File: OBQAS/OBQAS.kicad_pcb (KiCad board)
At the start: 2 copper layers, 151 x 100 mm, 146 parts, among them J1 24V IN, J2 USB_C_Receptacle_USB2.0, J3 K type, J5 TF_PUSH, J6 CH1, J7 CH2, K1 G5NB-1A-E_DC5, K2 G5NB-1A-E_DC5, K3 G5NB-1A-E_DC5, K4 G5NB-1A-E_DC5, Q1 IRLML2803TRPBF, Q2 IRLML2803TRPBF, Q3 IRLML2803TRPBF, Q4 IRLML2803TRPBF, Q5 BC846, Q6 BC846, Q7 IRLZ44N, Q8 IRLZ44N, Q9 IRFP064, SW1 SW_SPST, SW2 Enc, U1 LM7805_TO220, U2 AMS1117-3.3, U3 ESP32-WROOM-32, U4 CH340C, U5 TPS55288QWRPMRQ1, U6 LM358, U7 LM358, U8 MCP4921, U9 ADS1115IDGS

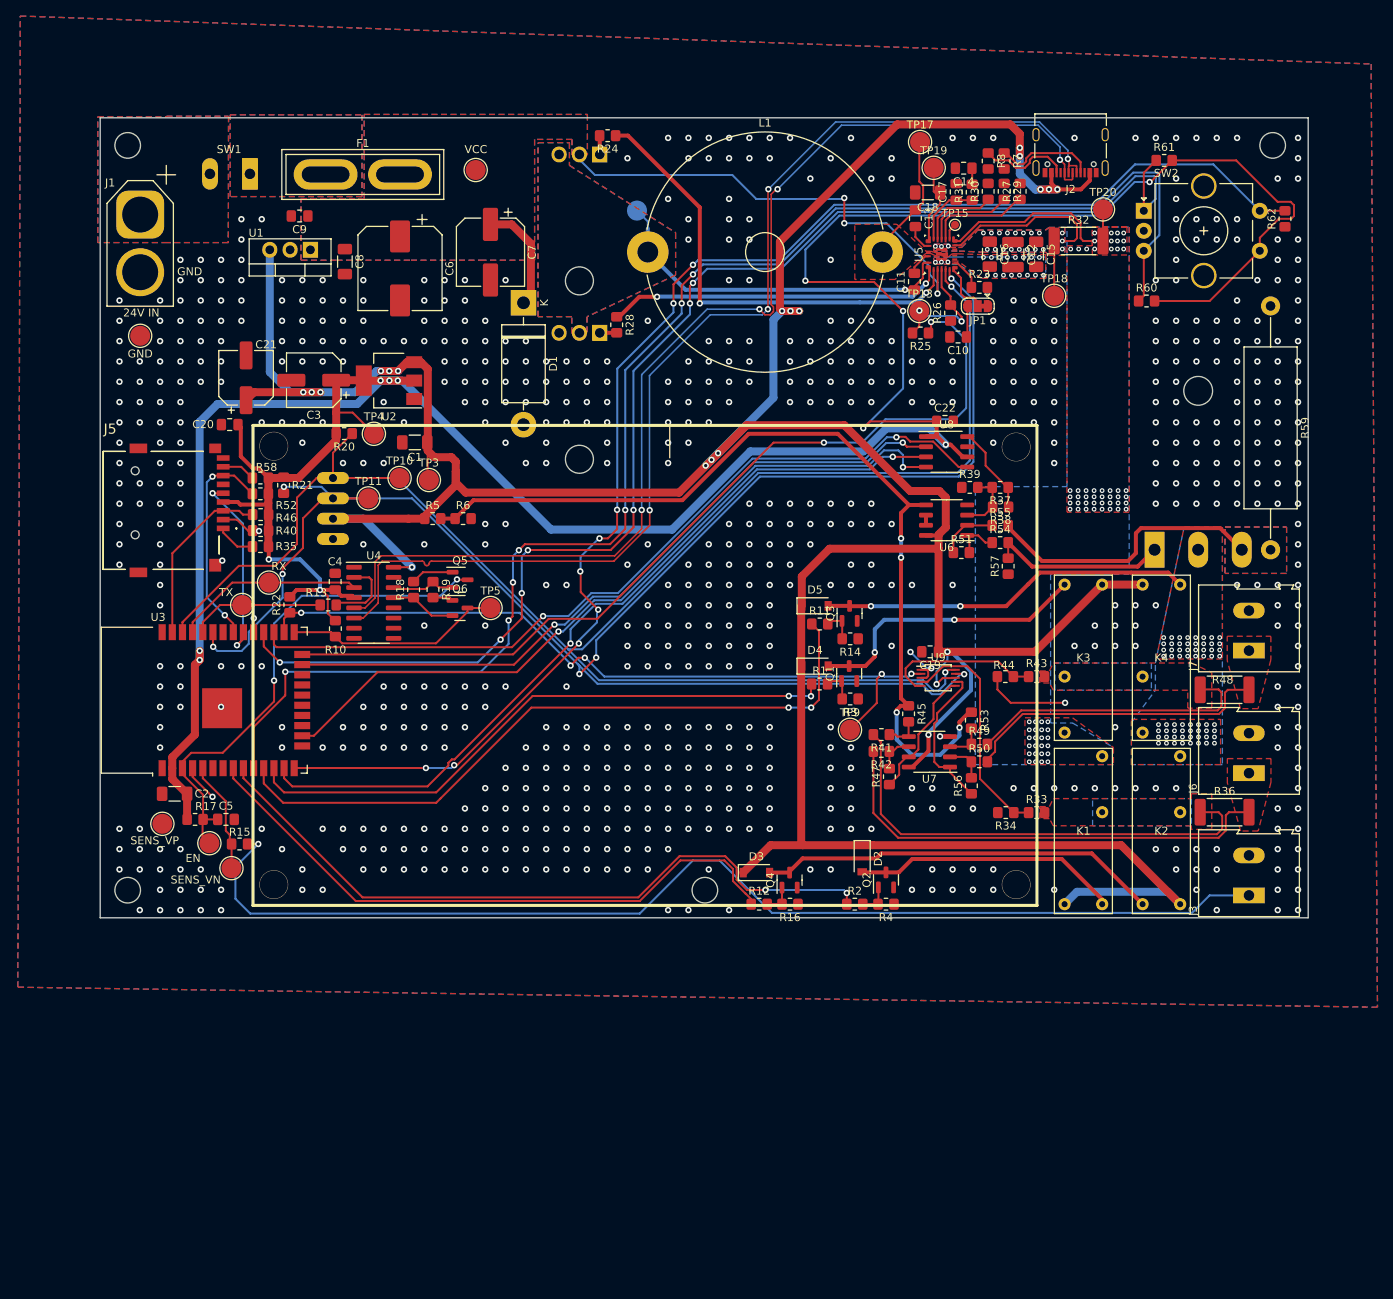
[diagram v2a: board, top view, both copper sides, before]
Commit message: updated schematic with balancing circuit
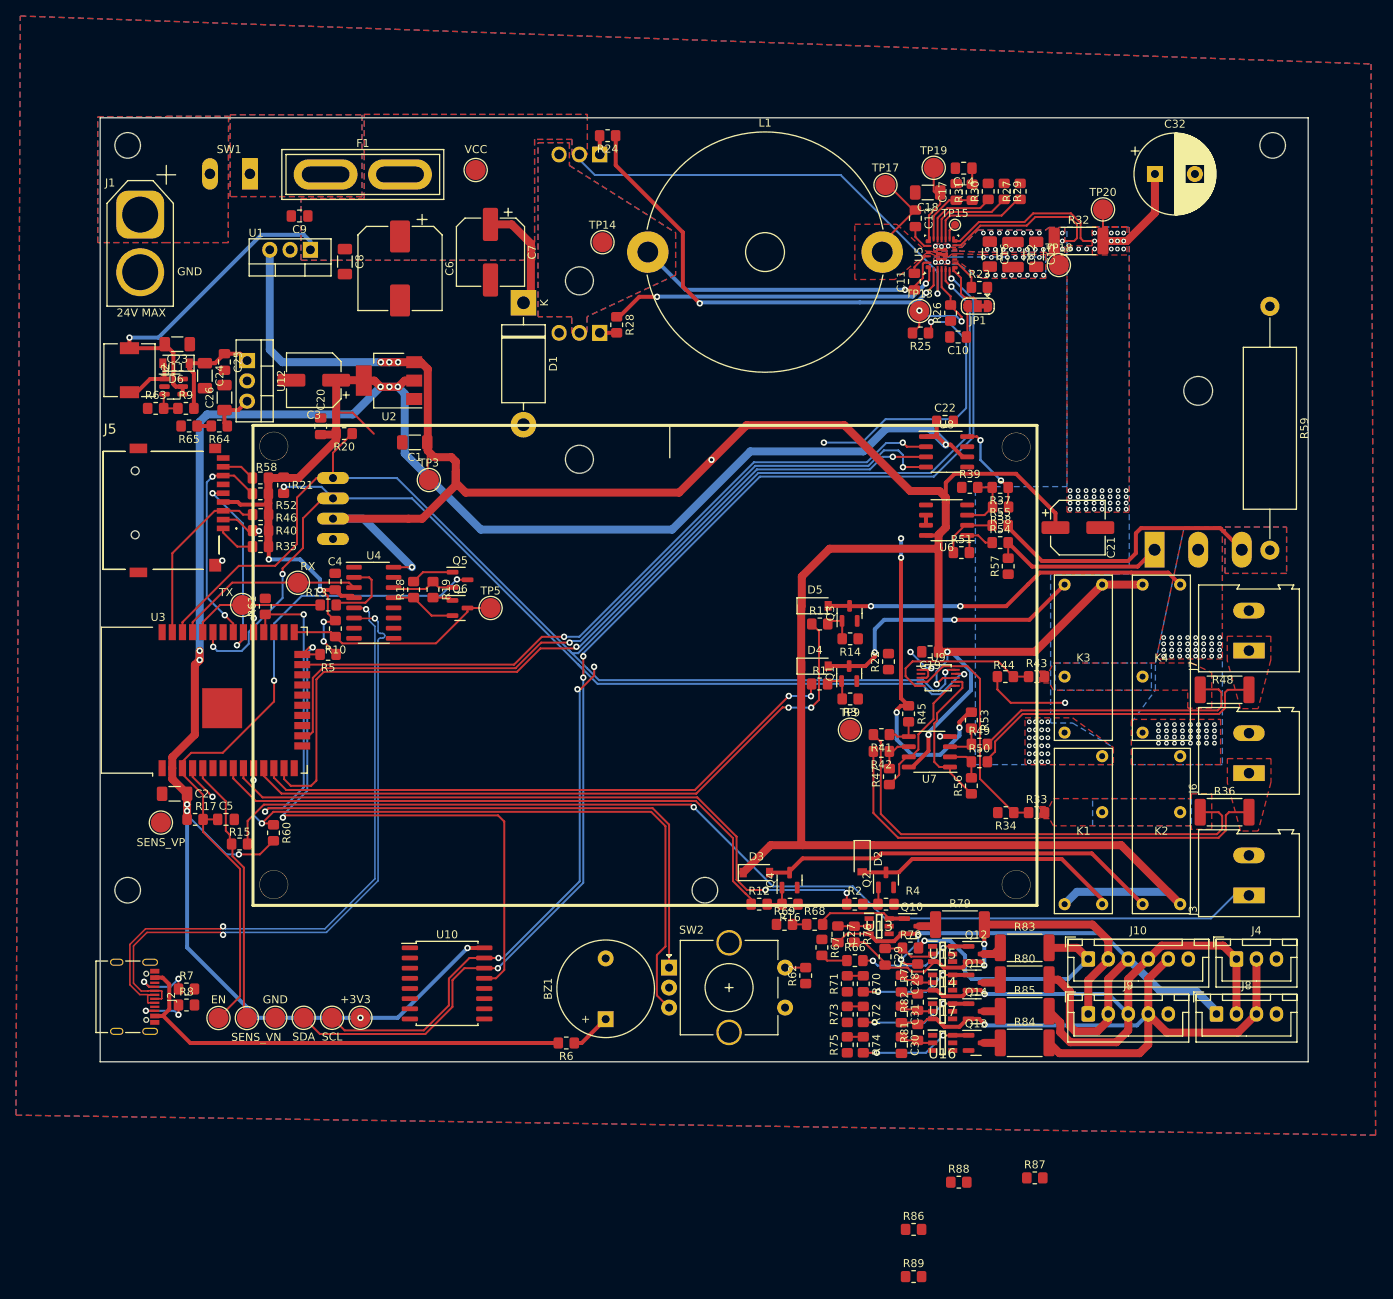
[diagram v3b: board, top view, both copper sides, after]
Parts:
- added BZ1: Buzzer, Buzzer_Beeper:Buzzer_12x9.5RM7.6, F.Cu at (132.6, 155.0)
- added C23: 10u, Capacitor_SMD:C_1206_3216Metric_Pad1.33x1.80mm_HandSolder, F.Cu at (79.1, 70.6)
- added C24: 10u, Capacitor_SMD:C_1206_3216Metric_Pad1.33x1.80mm_HandSolder, F.Cu at (82.5, 74.5)
- added C25: 100n, Capacitor_SMD:C_0805_2012Metric_Pad1.18x1.45mm_HandSolder, F.Cu at (85.0, 72.8)
- added C26: 10u, Capacitor_SMD:C_1206_3216Metric_Pad1.33x1.80mm_HandSolder, F.Cu at (85.0, 77.3)
- added C27: 100n, Capacitor_SMD:C_0805_2012Metric_Pad1.18x1.45mm_HandSolder, F.Cu at (161.7, 144.4)
- added C28: 100n, Capacitor_SMD:C_0805_2012Metric_Pad1.18x1.45mm_HandSolder, F.Cu at (169.6, 150.5)
- added C29: 100n, Capacitor_SMD:C_0805_2012Metric_Pad1.18x1.45mm_HandSolder, F.Cu at (167.6, 147.2)
- added C30: 100n, Capacitor_SMD:C_0805_2012Metric_Pad1.18x1.45mm_HandSolder, F.Cu at (169.6, 158.2)
- added C31: 100n, Capacitor_SMD:C_0805_2012Metric_Pad1.18x1.45mm_HandSolder, F.Cu at (169.6, 154.4)
- added C32: 1000u, Capacitor_THT:CP_Radial_D10.0mm_P5.00mm, F.Cu at (201.3, 49.3)
- added D6: 1N4001, Diode_SMD:D_SOD-123, F.Cu at (78.9, 73.0)
- added J10: Conn_01x06, Connector_JST:JST_XH_B6B-XH-A_1x06_P2.50mm_Vertical, F.Cu at (192.9, 147.4)
- added J4: Conn_01x03, Connector_JST:JST_XH_B3B-XH-A_1x03_P2.50mm_Vertical, F.Cu at (211.5, 147.4)
- added J8: Conn_01x04, Connector_JST:JST_XH_B4B-XH-A_1x04_P2.50mm_Vertical, F.Cu at (209.0, 154.3)
- added J9: Conn_01x05, Connector_JST:JST_XH_B5B-XH-A_1x05_P2.50mm_Vertical, F.Cu at (192.9, 154.3)
- added L2: 22uH, Inductor_SMD:L_6.3x6.3_H3, F.Cu at (73.1, 73.8)
- added Q10: IRLML2803TRPBF, Package_TO_SOT_SMD:SOT-23, F.Cu at (170.9, 143.3)
- added Q11: IRLML2803TRPBF, Package_TO_SOT_SMD:SOT-23, F.Cu at (178.9, 150.4)
- added Q12: IRLML2803TRPBF, Package_TO_SOT_SMD:SOT-23, F.Cu at (178.9, 146.8)
- added Q13: IRLML2803TRPBF, Package_TO_SOT_SMD:SOT-23, F.Cu at (178.9, 157.9)
- added Q14: IRLML2803TRPBF, Package_TO_SOT_SMD:SOT-23, F.Cu at (178.9, 154.0)
- added R63: 1k, Resistor_SMD:R_0805_2012Metric_Pad1.20x1.40mm_HandSolder, F.Cu at (76.4, 78.6)
- added R64: 5.1k, Resistor_SMD:R_0805_2012Metric_Pad1.20x1.40mm_HandSolder, F.Cu at (84.3, 80.8)
- added R65: 5.1k, Resistor_SMD:R_0805_2012Metric_Pad1.20x1.40mm_HandSolder, F.Cu at (80.5, 80.8)
- added R66: 10k, Resistor_SMD:R_0805_2012Metric_Pad1.20x1.40mm_HandSolder, F.Cu at (163.8, 147.7)
- added R67: 10k, Resistor_SMD:R_0805_2012Metric_Pad1.20x1.40mm_HandSolder, F.Cu at (159.7, 146.0)
- added R68: 50k, Resistor_SMD:R_0805_2012Metric_Pad1.20x1.40mm_HandSolder, F.Cu at (158.8, 143.1)
- added R69: 10k, Resistor_SMD:R_0805_2012Metric_Pad1.20x1.40mm_HandSolder, F.Cu at (155.0, 143.1)
- added R70: 50k, Resistor_SMD:R_0805_2012Metric_Pad1.20x1.40mm_HandSolder, F.Cu at (164.8, 150.6)
- added R71: 10k, Resistor_SMD:R_0805_2012Metric_Pad1.20x1.40mm_HandSolder, F.Cu at (162.8, 150.6)
- added R72: 20k, Resistor_SMD:R_0805_2012Metric_Pad1.20x1.40mm_HandSolder, F.Cu at (164.8, 154.4)
- added R73: 10k, Resistor_SMD:R_0805_2012Metric_Pad1.20x1.40mm_HandSolder, F.Cu at (162.8, 154.4)
- added R74: 10k, Resistor_SMD:R_0805_2012Metric_Pad1.20x1.40mm_HandSolder, F.Cu at (164.8, 158.2)
- added R75: 10k, Resistor_SMD:R_0805_2012Metric_Pad1.20x1.40mm_HandSolder, F.Cu at (162.8, 158.2)
- added R76: 100, Resistor_SMD:R_0805_2012Metric_Pad1.20x1.40mm_HandSolder, F.Cu at (163.7, 144.3)
- added R77: 100, Resistor_SMD:R_0805_2012Metric_Pad1.20x1.40mm_HandSolder, F.Cu at (171.6, 149.1)
- added R78: 100, Resistor_SMD:R_0805_2012Metric_Pad1.20x1.40mm_HandSolder, F.Cu at (170.7, 146.1)
- added R79: 10, Resistor_SMD:R_2512_6332Metric_Pad1.40x3.35mm_HandSolder, F.Cu at (176.9, 143.1)
- added R80: 10, Resistor_SMD:R_2512_6332Metric_Pad1.40x3.35mm_HandSolder, F.Cu at (185.0, 150.0)
- added R81: 100, Resistor_SMD:R_0805_2012Metric_Pad1.20x1.40mm_HandSolder, F.Cu at (171.6, 156.6)
- added R82: 100, Inductor_SMD:L_0805_2012Metric_Pad1.15x1.40mm_HandSolder, F.Cu at (171.6, 152.8)
- added R83: 10, Resistor_SMD:R_2512_6332Metric_Pad1.40x3.35mm_HandSolder, F.Cu at (185.0, 146.1)
- added R84: 10, Resistor_SMD:R_2512_6332Metric_Pad1.40x3.35mm_HandSolder, F.Cu at (185.0, 157.9)
- added R85: 10, Resistor_SMD:R_2512_6332Metric_Pad1.40x3.35mm_HandSolder, F.Cu at (185.0, 154.0)
- added R86: 50k, Resistor_SMD:R_0805_2012Metric_Pad1.20x1.40mm_HandSolder, F.Cu at (171.1, 181.2)
- added R87: 10k, Resistor_SMD:R_0805_2012Metric_Pad1.20x1.40mm_HandSolder, F.Cu at (186.3, 174.8)
- added R88: 50k, Resistor_SMD:R_0805_2012Metric_Pad1.20x1.40mm_HandSolder, F.Cu at (176.8, 175.3)
- added R89: 10k, Resistor_SMD:R_0805_2012Metric_Pad1.20x1.40mm_HandSolder, F.Cu at (171.1, 187.2)
- added R9: 50k, Resistor_SMD:R_0805_2012Metric_Pad1.20x1.40mm_HandSolder, F.Cu at (80.2, 78.6)
- added U10: PCF8574, Package_SO:SOIC-16W_7.5x10.3mm_P1.27mm, F.Cu at (112.8, 150.5)
- added U11: MT3608, Package_TO_SOT_SMD:SOT-23-6, F.Cu at (78.6, 75.9)
- added U12: LM7824_TO220, Package_TO_SOT_THT:TO-220-3_Vertical, F.Cu at (87.8, 72.6)
- added U13: HY2213-BB3A, HY2213:SOT95P280X140-6N, F.Cu at (166.8, 143.3)
- added U14: HY2213-BB3A, HY2213:SOT95P280X140-6N, F.Cu at (174.7, 150.4)
- added U15: HY2213-BB3A, HY2213:SOT95P280X140-6N, F.Cu at (174.7, 146.8)
- added U16: HY2213-BB3A, HY2213:SOT95P280X140-6N, F.Cu at (174.8, 157.9)
- added U17: HY2213-BB3A, HY2213:SOT95P280X140-6N, F.Cu at (174.7, 154.0)
- J1: value 24V IN -> 24V MAX
- R5: value 470 -> 10k
- TP14: moved to F.Cu
- moved J2 157.5 mm to (73.8, 152.2), turned to -90 degrees
- moved R8 145.5 mm to (80.2, 153.2), turned to 0 degrees
- moved R7 145.5 mm to (80.2, 151.2), turned to 0 degrees
- moved R60 127.8 mm to (91.1, 131.7), turned to -90 degrees
- moved R61 125.4 mm to (90.1, 103.4), turned to 90 degrees
- moved R62 112.0 mm to (157.6, 149.5)
- moved SW2 111.7 mm to (140.6, 148.5)
- moved C21 105.6 mm to (191.7, 93.5), turned to 0 degrees
- moved TP16 86.9 mm to (91.3, 154.8)
- moved R22 75.2 mm to (168.0, 110.3)
- moved TP4 73.0 mm to (102.0, 154.8)
- moved TP10 68.0 mm to (98.4, 154.8)
- moved R6 66.8 mm to (127.7, 157.9), turned to 180 degrees
- moved TP11 65.4 mm to (94.9, 154.8)
- moved TP6 21.9 mm to (84.2, 154.8)
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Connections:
- R45 pad 1: +2V5 -> +12V
- R5 pad 1: +5V -> +3V3
- R5 pad 2: +2V5 -> PCF_INT
- R53 pad 1: +2V5 -> +12V
- R6 pad 1: +2V5 -> Net-(BZ1-Pad1)
- R6 pad 2: GND -> +5V
- U3 pad 14: ENC_Button -> 2S_ADC
- U3 pad 24: EN_UVLDO -> PCF_INT
- U3 pad 26: ADC_READY -> 1S_ADC
- U3 pad 27: DAC_LDAC -> 3S_ADC
- U3 pad 6: unconnected-(U3-Pad6) -> 4S_ADC
- U3 pad 7: unconnected-(U3-Pad7) -> 5S_ADC
- U6 pad 5: +2V5 -> +3V3
- U7 pad 8: +5V -> +24V
- U9 pad 6: CH1_ADC_I -> Net-(R88-Pad1)
- U9 pad 7: CH2_ADC_I -> Net-(R86-Pad1)
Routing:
- net ENC_Button: track 179.4 -> 2.57 mm, vias 9 -> 0
- net +2V5: track 113.4 -> 0.00 mm, vias 4 -> 0
- net ENC_B: track 185.6 -> 84.4 mm, vias 7 -> 2
- net DAC_LDAC: track 100.8 -> 0.00 mm, vias 2 -> 0
- net ADC_READY: track 94.9 -> 0.00 mm, vias 5 -> 0
- net BAT_3S: track 0.00 -> 81.2 mm, vias 0 -> 2
- net BAT_1S: track 0.00 -> 80.4 mm, vias 0 -> 1
- net PCF_INT: track 0.00 -> 76.3 mm, vias 0 -> 2
- net EN_UVLDO: track 111.1 -> 34.9 mm
- net BAT_2S: track 0.00 -> 72.6 mm, vias 0 -> 1
- net SDA: track 221.5 -> 287.4 mm, vias 7 -> 8
- net ENC_A: track 169.1 -> 104.2 mm, vias 7 -> 2
- net /D-: track 144.2 -> 81.3 mm, vias 4 -> 2
- net /D+: track 144.0 -> 81.4 mm, vias 4 -> 2
- net +3V3: track 390.3 -> 329.0 mm, vias 12 -> 15
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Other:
- board size 151 x 100 mm -> 151 x 118 mm

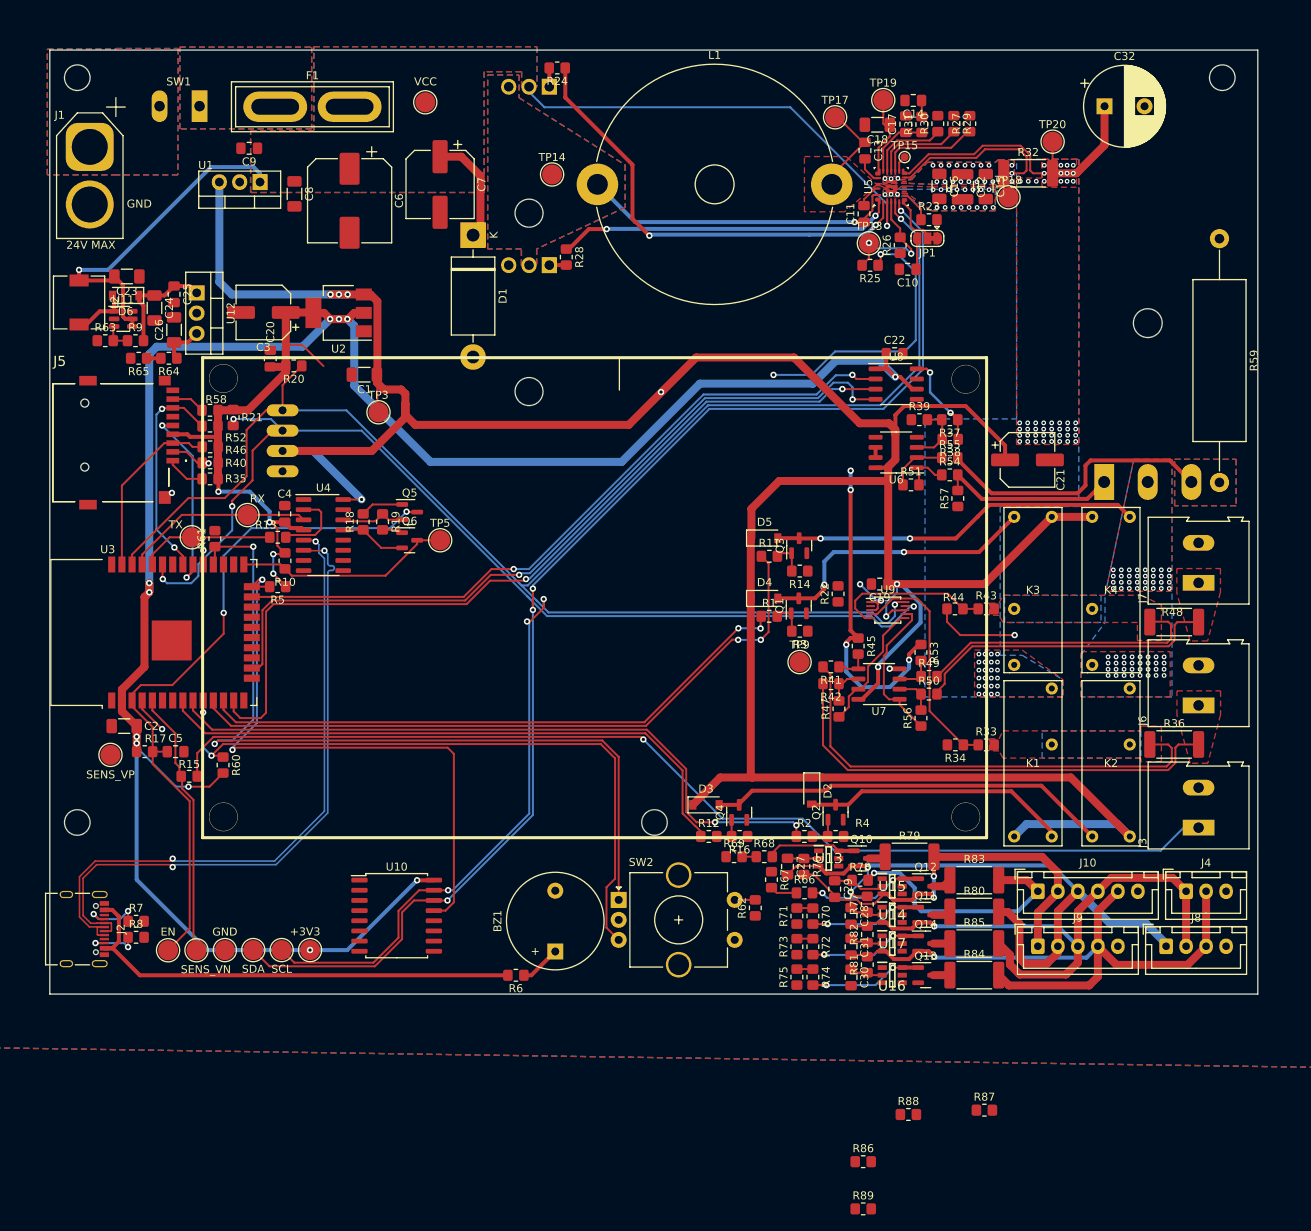
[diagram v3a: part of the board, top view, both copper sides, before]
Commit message: finished routing of the new circuit
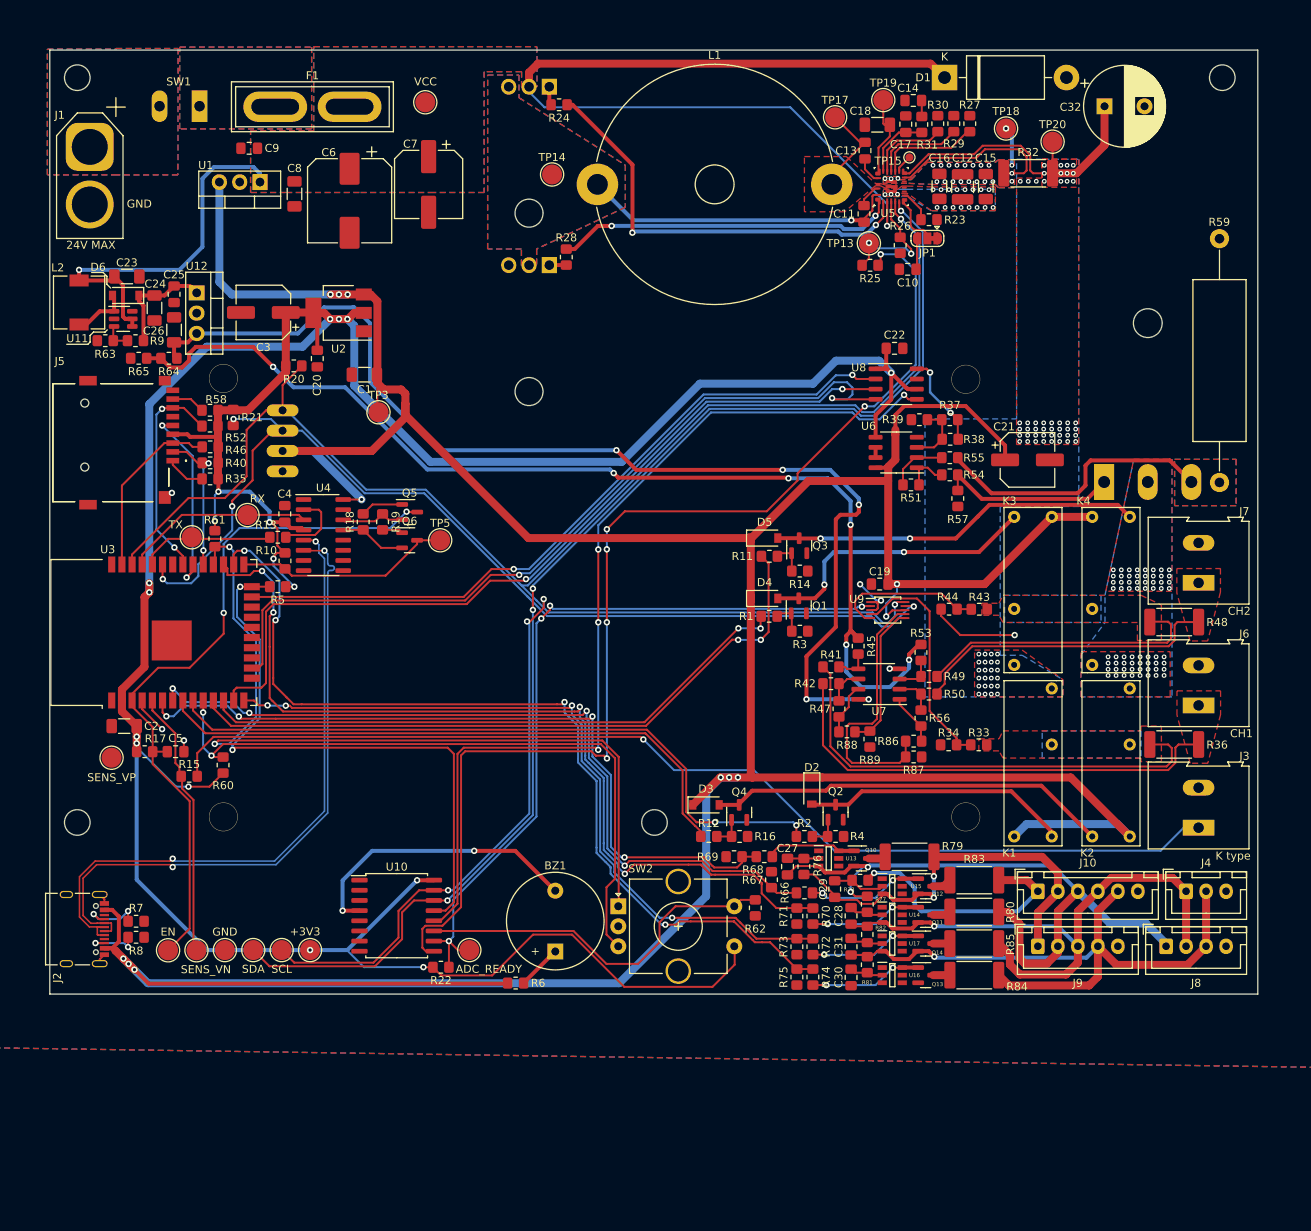
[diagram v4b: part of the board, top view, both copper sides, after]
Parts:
- moved R22 68.1 mm to (118.3, 156.9), turned to 180 degrees
- moved D1 62.1 mm to (181.3, 45.7), turned to 0 degrees
- moved R89 58.7 mm to (171.9, 128.4), turned to -90 degrees
- moved TP9 54.8 mm to (121.9, 154.8)
- moved R86 52.9 mm to (177.4, 128.7)
- moved R88 48.4 mm to (169.1, 127.5), turned to 180 degrees
- moved R87 45.0 mm to (177.4, 130.7)
- moved TP18 8.60 mm to (189.0, 52.1)
- moved C20 5.88 mm to (102.9, 80.9), turned to 90 degrees
- moved R24 4.61 mm to (133.1, 49.1)
- moved C7 1.44 mm to (116.8, 59.1)
- moved R6 0.98 mm to (127.7, 158.9)
- moved R33 0.93 mm to (185.6, 129.1)
- moved R43 0.87 mm to (185.6, 112.2)
- moved R34 0.85 mm to (181.8, 129.1)
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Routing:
- net +24V: track 5.42 -> 141.8 mm, vias 0 -> 5
- net DAC_LDAC: track 0.00 -> 116.2 mm, vias 0 -> 4
- net 1S_ADC: track 2.00 -> 114.0 mm, vias 0 -> 4
- net 3S_ADC: track 2.00 -> 112.9 mm, vias 0 -> 4
- net EN_UVLDO: track 34.9 -> 142.5 mm, vias 2 -> 6
- net 5S_ADC: track 3.39 -> 99.6 mm, vias 0 -> 4
- net ADC_READY: track 0.00 -> 95.7 mm, vias 0 -> 4
- net +12V: track 41.8 -> 135.5 mm, vias 4 -> 6
- net 4S_ADC: track 1.78 -> 94.2 mm, vias 0 -> 4
- net 2S_ADC: track 2.00 -> 92.8 mm, vias 0 -> 4
- net +3V3: track 329.0 -> 395.8 mm, vias 15 -> 17
- net +5V: track 444.3 -> 500.3 mm, vias 8 -> 12
- net VCC: track 113.8 -> 159.9 mm
- net ENC_Button: track 2.57 -> 46.7 mm
- net Net-(BZ1-Pad2): track 0.00 -> 36.1 mm, vias 0 -> 2
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
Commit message: final PCB
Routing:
- net 4S_ADC: track 94.2 -> 96.2 mm
- net 5S_ADC: track 99.6 -> 101.2 mm
- net 3S_ADC: track 112.9 -> 114.0 mm
- net +5V: track 500.3 -> 499.7 mm
- net GND: vias 26 -> 954
